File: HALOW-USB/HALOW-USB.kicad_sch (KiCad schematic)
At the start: 12 parts, among them U1 TLV75533PDBVR, U2 GT-USB-7010ASV

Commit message: trace work
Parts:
- removed U2: GT-USB-7010ASV, easyeda2kicad:USB-C-SMD_G-SWITCH_GT-USB-7010ASV, symbol easyeda2kicad:GT-USB-7010ASV
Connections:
- net 5v_in renamed +5V
- net USB_D+ renamed USB/USB_D+
- net USB_D- renamed USB/USB D-
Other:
- added sheet USB (USB.kicad_sch)

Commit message: mfg files added
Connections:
- net USB/USB D- renamed D -
- net USB/USB_D+ renamed D +
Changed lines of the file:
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@@
+		)
+	)
+	(label "D -"
+		(at 68.58 78.74 0)
+		(effects
+			(font
+				(size 1.27 1.27)
+			)
+			(justify left bottom)
+		)
+	)
+	(label "D +"
+		(at 68.58 81.28 0)
+		(effects
+			(font
+				(size 1.27 1.27)
+			)
+			(justify left bottom)
 		)
 	)

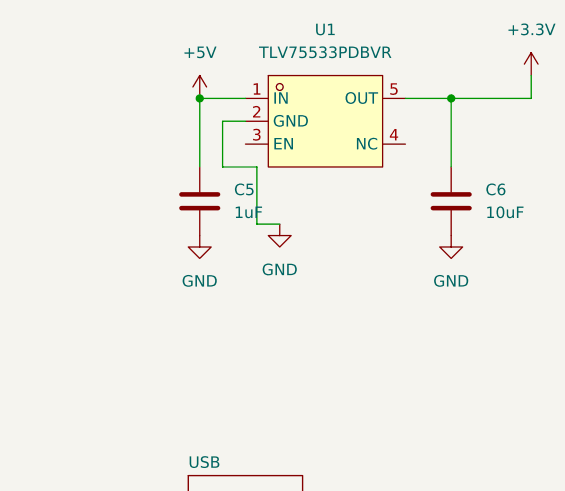
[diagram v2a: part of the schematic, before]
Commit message: added 5v enable and stp export
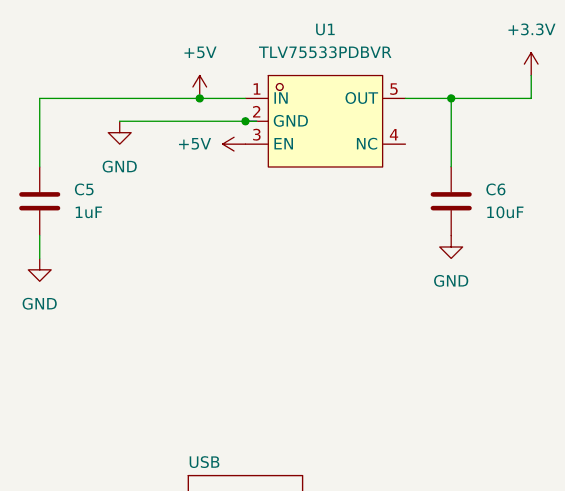
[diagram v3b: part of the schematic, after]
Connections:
- net +5V: now also U1.3 (EN)
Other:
- moved on the sheet: C5
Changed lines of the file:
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@@
+	)
+	(junction
+		(at 48.26 31.75)
+		(diameter 0)
+		(color 0 0 0 0)
 	)
 	(junction
@@
 	)
 	(junction
-		(at 48.26 31.75)
-		(diameter 0)
-		(color 0 0 0 0)
-	)
-	(junction
 		(at 76.2 31.75)
 		(diameter 0)
@@
 	)
 	(junction
+		(at 53.34 34.29)
+		(diameter 0)
+		(color 0 0 0 0)
+	)
+	(junction
 		(at 146.05 88.9)
 		(diameter 0)
@@
 	(wire
 		(pts
-			(xy 54.61 45.72) (xy 57.15 45.72)
+			(xy 30.48 49.53) (xy 30.48 46.99)
+		)
+		(stroke
+			(width 0)
+			(type default)
+		)
+	)
+	(wire
+		(pts
+			(xy 54.61 34.29) (xy 53.34 34.29)
 		)
 		(stroke
@@
 	(wire
 		(pts
-			(xy 53.34 34.29) (xy 50.8 34.29)
+			(xy 39.37 34.29) (xy 53.34 34.29)
 		)
 		(stroke
@@
 	(wire
 		(pts
-			(xy 54.61 39.37) (xy 54.61 45.72)
-		)
-		(stroke
-			(width 0)
-			(type default)
-		)
-	)
-	(wire
-		(pts
 			(xy 116.84 129.54) (xy 118.11 129.54)
 		)
@@
 	(wire
 		(pts
-			(xy 50.8 39.37) (xy 54.61 39.37)
-		)
-		(stroke
-			(width 0)
-			(type default)
-		)
-	)
-	(wire
-		(pts
 			(xy 81.28 119.38) (xy 81.28 120.65)
 		)
@@
 	(wire
 		(pts
+			(xy 48.26 31.75) (xy 53.34 31.75)
+		)
+		(stroke
+			(width 0)
+			(type default)
+		)
+	)
+	(wire
+		(pts
 			(xy 114.3 129.54) (xy 116.84 129.54)
 		)
@@
 	(wire
 		(pts
-			(xy 50.8 34.29) (xy 50.8 39.37)
-		)
-		(stroke
-			(width 0)
-			(type default)
-		)
-	)
-	(wire
-		(pts
 			(xy 146.05 88.9) (xy 148.59 88.9)
 		)
@@
 	(wire
 		(pts
-			(xy 48.26 39.37) (xy 48.26 31.75)
-		)
-		(stroke
-			(width 0)
-			(type default)
-		)
-	)
-	(wire
-		(pts
-			(xy 48.26 31.75) (xy 53.34 31.75)
+			(xy 30.48 31.75) (xy 30.48 39.37)
+		)
+		(stroke
+			(width 0)
+			(type default)
+		)
+	)
+	(wire
+		(pts
+			(xy 30.48 31.75) (xy 48.26 31.75)
 		)
 		(stroke
@@
 	(symbol
 		(lib_id "power:GND")
-		(at 48.26 46.99 0)
+		(at 30.48 49.53 0)
 		(unit 1)
 		(exclude_from_sim no)
@@
 		(fields_autoplaced yes)
 		(property "Reference" "#PWR09"
-			(at 48.26 53.34 0)
+			(at 30.48 55.88 0)
 			(effects
 				(font
@@
 		)
 		(property "Value" "GND"
-			(at 48.26 52.07 0)
+			(at 30.48 54.61 0)
 			(effects
 				(font
@@
 		)
 		(property "Footprint" ""
-			(at 48.26 46.99 0)
+			(at 30.48 49.53 0)
 			(effects
 				(font
@@
 		)
 		(property "Datasheet" ""
-			(at 48.26 46.99 0)
+			(at 30.48 49.53 0)
 			(effects
 				(font
@@
 		)
 		(property "Description" "Power symbol creates a global label with name \"GND\" , ground"
-			(at 48.26 46.99 0)
+			(at 30.48 49.53 0)
 			(effects
 				(font
@@
 	(symbol
 		(lib_id "power:GND")
-		(at 57.15 45.72 0)
+		(at 39.37 34.29 0)
 		(unit 1)
 		(exclude_from_sim no)
@@
 		(fields_autoplaced yes)
 		(property "Reference" "#PWR016"
-			(at 57.15 52.07 0)
+			(at 39.37 40.64 0)
 			(effects
 				(font
@@
 		)
 		(property "Value" "GND"
-			(at 57.15 50.8 0)
+			(at 39.37 39.37 0)
 			(effects
 				(font
@@
 		)
 		(property "Footprint" ""
-			(at 57.15 45.72 0)
+			(at 39.37 34.29 0)
 			(effects
 				(font
@@
 		)
 		(property "Datasheet" ""
-			(at 57.15 45.72 0)
+			(at 39.37 34.29 0)
 			(effects
 				(font
@@
 		)
 		(property "Description" "Power symbol creates a global label with name \"GND\" , ground"
-			(at 57.15 45.72 0)
+			(at 39.37 34.29 0)
 			(effects
 				(font
@@
 	(symbol
 		(lib_id "Device:C")
-		(at 48.26 43.18 0)
+		(at 30.48 43.18 0)
 		(unit 1)
 		(exclude_from_sim no)
@@
 		(fields_autoplaced yes)
 		(property "Reference" "C5"
-			(at 52.07 41.9099 0)
+			(at 34.29 41.9099 0)
 			(effects
 				(font
@@
 		)
 		(property "Value" "1uF"
-			(at 52.07 44.4499 0)
+			(at 34.29 44.4499 0)
 			(effects
 				(font
@@
 		)
 		(property "Footprint" "Capacitor_SMD:C_0603_1608Metric_Pad1.08x0.95mm_HandSolder"
-			(at 49.2252 46.99 0)
+			(at 31.4452 46.99 0)
 			(effects
 				(font
@@
 		)
 		(property "Datasheet" "~"
-			(at 48.26 43.18 0)
+			(at 30.48 43.18 0)
 			(effects
 				(font
@@
 		)
 		(property "Description" "Unpolarized capacitor"
-			(at 48.26 43.18 0)
+			(at 30.48 43.18 0)
 			(effects
 				(font
@@
 					(unit 1)
 				)
+			)
+		)
+	)
+	(symbol
+		(lib_id "power:+5V")
+		(at 53.34 36.83 90)
+		(unit 1)
+		(exclude_from_sim no)
+		(in_bom yes)
+		(on_board yes)
+		(dnp no)
+		(fields_autoplaced yes)
+		(property "Reference" "#PWR028"
+			(at 57.15 36.83 0)
+			(effects
+				(font
+					(size 1.27 1.27)
+				)
+				(hide yes)
+			)
+		)
+		(property "Value" "+5V"
+			(at 49.53 36.8299 90)
+			(effects
+				(font
+					(size 1.27 1.27)
+				)
+				(justify left)
+			)
+		)
+		(property "Footprint" ""
+			(at 53.34 36.83 0)
+			(effects
+				(font
+					(size 1.27 1.27)
+				)
+				(hide yes)
+			)
+		)
+		(property "Datasheet" ""
+			(at 53.34 36.83 0)
+			(effects
+				(font
+					(size 1.27 1.27)
+				)
+				(hide yes)
+			)
+		)
+		(property "Description" "Power symbol creates a global label with name \"+5V\""
+			(at 53.34 36.83 0)
+			(effects
+				(font
+					(size 1.27 1.27)
+				)
+				(hide yes)
+			)
+		)
+		(pin "1"
+		)
+		(instances
+			(project ""
+				(path "/c461e236-6f15-491a-ad1b-e2a18f51e0df"
+					(reference "#PWR028")
+					(unit 1)
+				)
